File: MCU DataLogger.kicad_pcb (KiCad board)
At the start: 2 copper layers, 51 x 35 mm, 29 parts, among them J1 Conn_01x04_Pin, J2 Conn_01x09_Pin, J3 Conn_01x04_Pin, J4 Conn_02x03_Odd_Even, U1 24LC1025, U2 DS1337S_, U3 24LC1025, U4 ATMEGA328P-AU, Y1 32.768 KH, Y2 16MHz

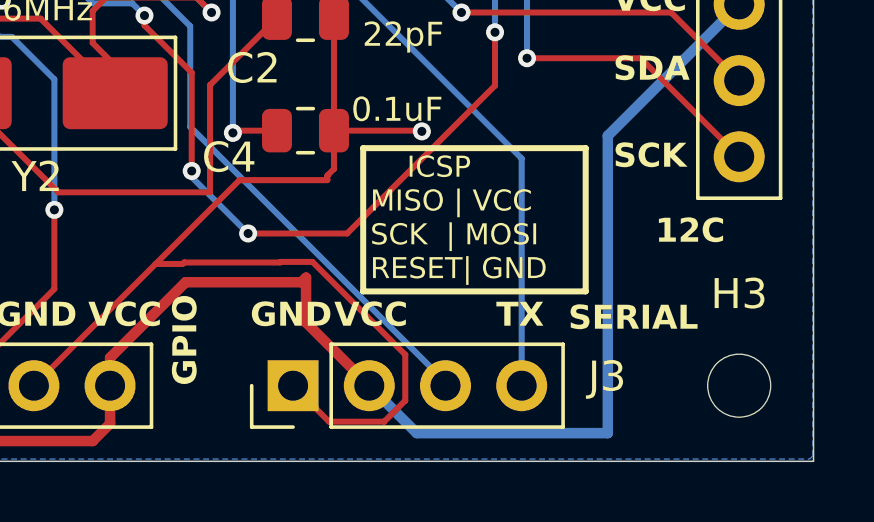
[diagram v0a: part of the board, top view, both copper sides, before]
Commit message: Added the missing RX label for J3 connector
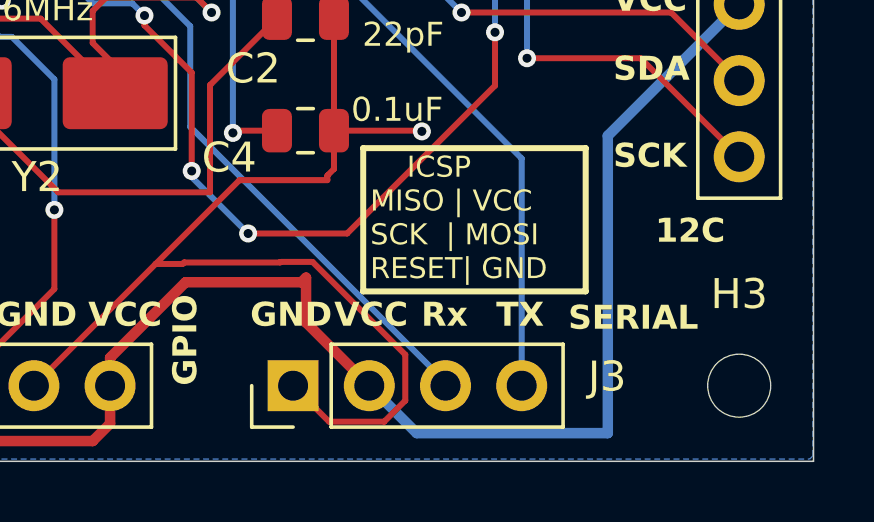
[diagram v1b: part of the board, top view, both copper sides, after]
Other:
- board text added: "Rx"
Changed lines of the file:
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@@
+		)
+	)
+	(gr_text "Rx"
+		(at 137.9 90.6 0)
+		(layer "F.SilkS")
+		(effects
+			(font
+				(size 0.8 0.8)
+				(thickness 0.15)
+				(bold yes)
+			)
+			(justify left bottom)
 		)
 	)

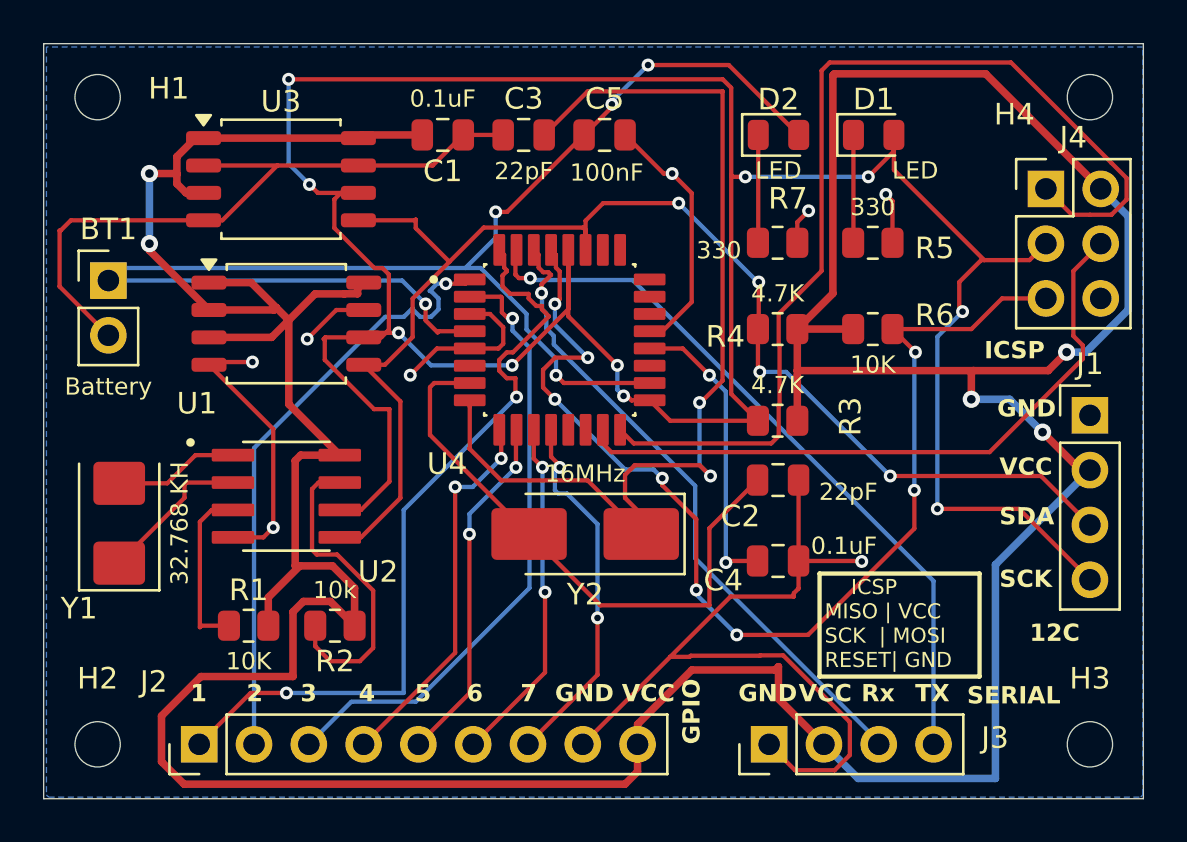
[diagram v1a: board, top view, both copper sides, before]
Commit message: Finished the 4layer routing
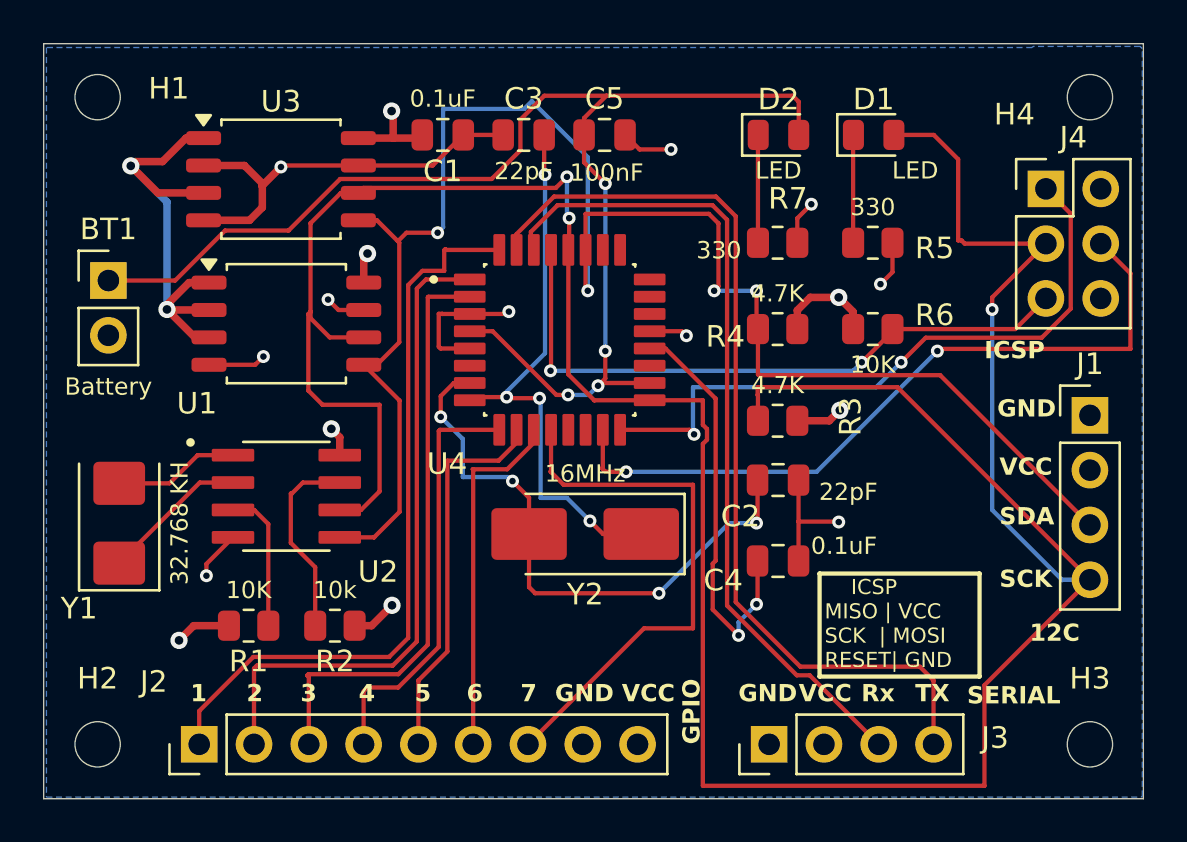
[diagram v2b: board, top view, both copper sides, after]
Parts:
- turned R1 to 180 degrees
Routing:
- net /Vcc: track 204.4 -> 41.0 mm, vias 5 -> 9
- net GND: track 107.8 -> 46.7 mm, vias 8 -> 10
- net /RESET: track 52.7 -> 30.0 mm, vias 8 -> 2
- net Net-(U4-PB7): track 47.2 -> 26.2 mm, vias 2 -> 4
- net /MISO: track 47.6 -> 30.8 mm, vias 0 -> 2
- net /SDA: track 64.3 -> 79.2 mm
- net /TX: track 34.0 -> 43.5 mm, vias 1 -> 0
- net /D8: track 17.2 -> 25.3 mm, vias 2 -> 0
- net /RX: track 30.3 -> 38.4 mm, vias 1 -> 0
- net /SCK: track 136.4 -> 143.4 mm, vias 10 -> 3
- net Net-(BT1-+): track 68.2 -> 62.2 mm, vias 5 -> 4
- net Net-(U2-SQW/~INT): track 14.7 -> 9.08 mm
- net Net-(U4-AREF): track 13.8 -> 19.4 mm
- net /MOSI: track 30.9 -> 34.2 mm, vias 0 -> 2
- net /D2: track 36.6 -> 34.5 mm, vias 2 -> 0
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- added copper zone on In1.Cu, net /Vcc
- added copper zone on In2.Cu, net /Vcc
- added copper zone on In1.Cu, net GND
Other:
- copper layers 2 -> 4
